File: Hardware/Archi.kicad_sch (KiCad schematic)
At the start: 13 parts, among them J3 Alimentación, J4 Analógico, J5 Digital/PWM, J6 Digital/PWM, U2 RESET

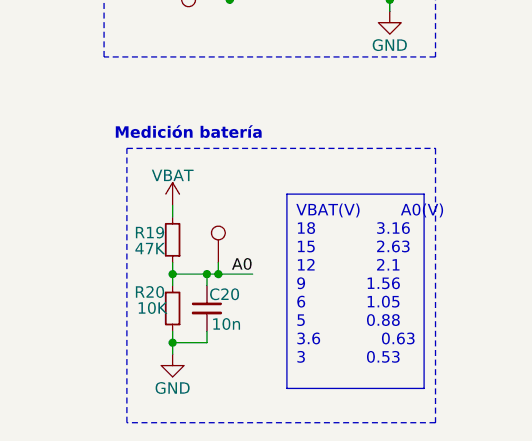
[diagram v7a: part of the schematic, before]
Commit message: Actualizo a version 1.3
- Footprint de conector compatible con 3 modelos (SMD, TH y bornera)
- Serigrafia en todos los componentes
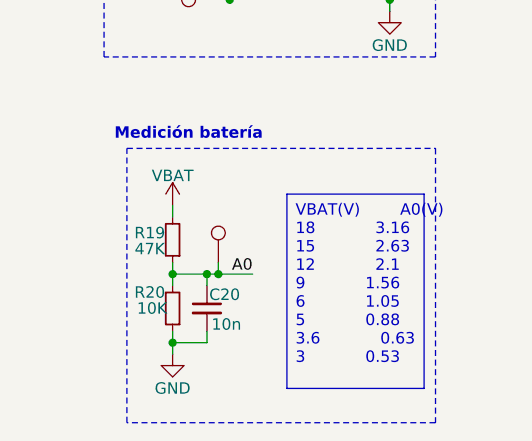
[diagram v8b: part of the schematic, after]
